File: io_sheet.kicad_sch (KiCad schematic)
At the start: 17 parts, among them J2 Conn_02x06_Top_Bottom, U1 PC817, U2 PC817, U3 PC817, U4 PC817, U5 PC817, U6 PC817, U7 PC817, U8 PC817

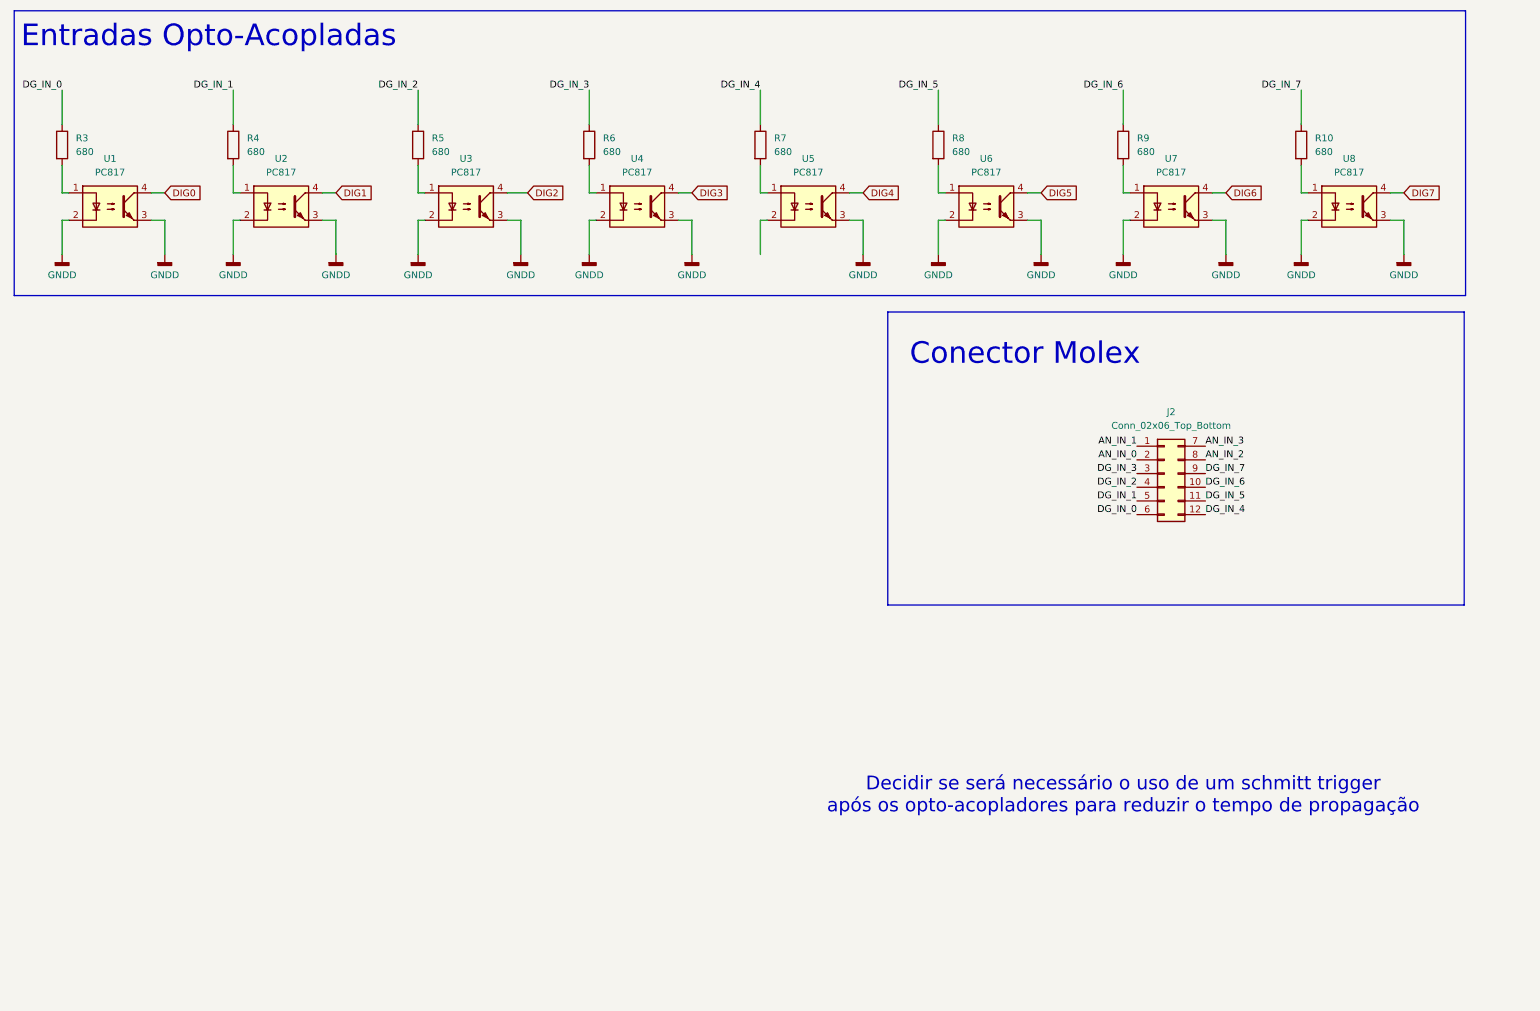
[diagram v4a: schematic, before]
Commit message: Alterei para ter 3 portas analogicas, adaptei o circuito do RPM para ter um jumper que permite usar como entrada digital
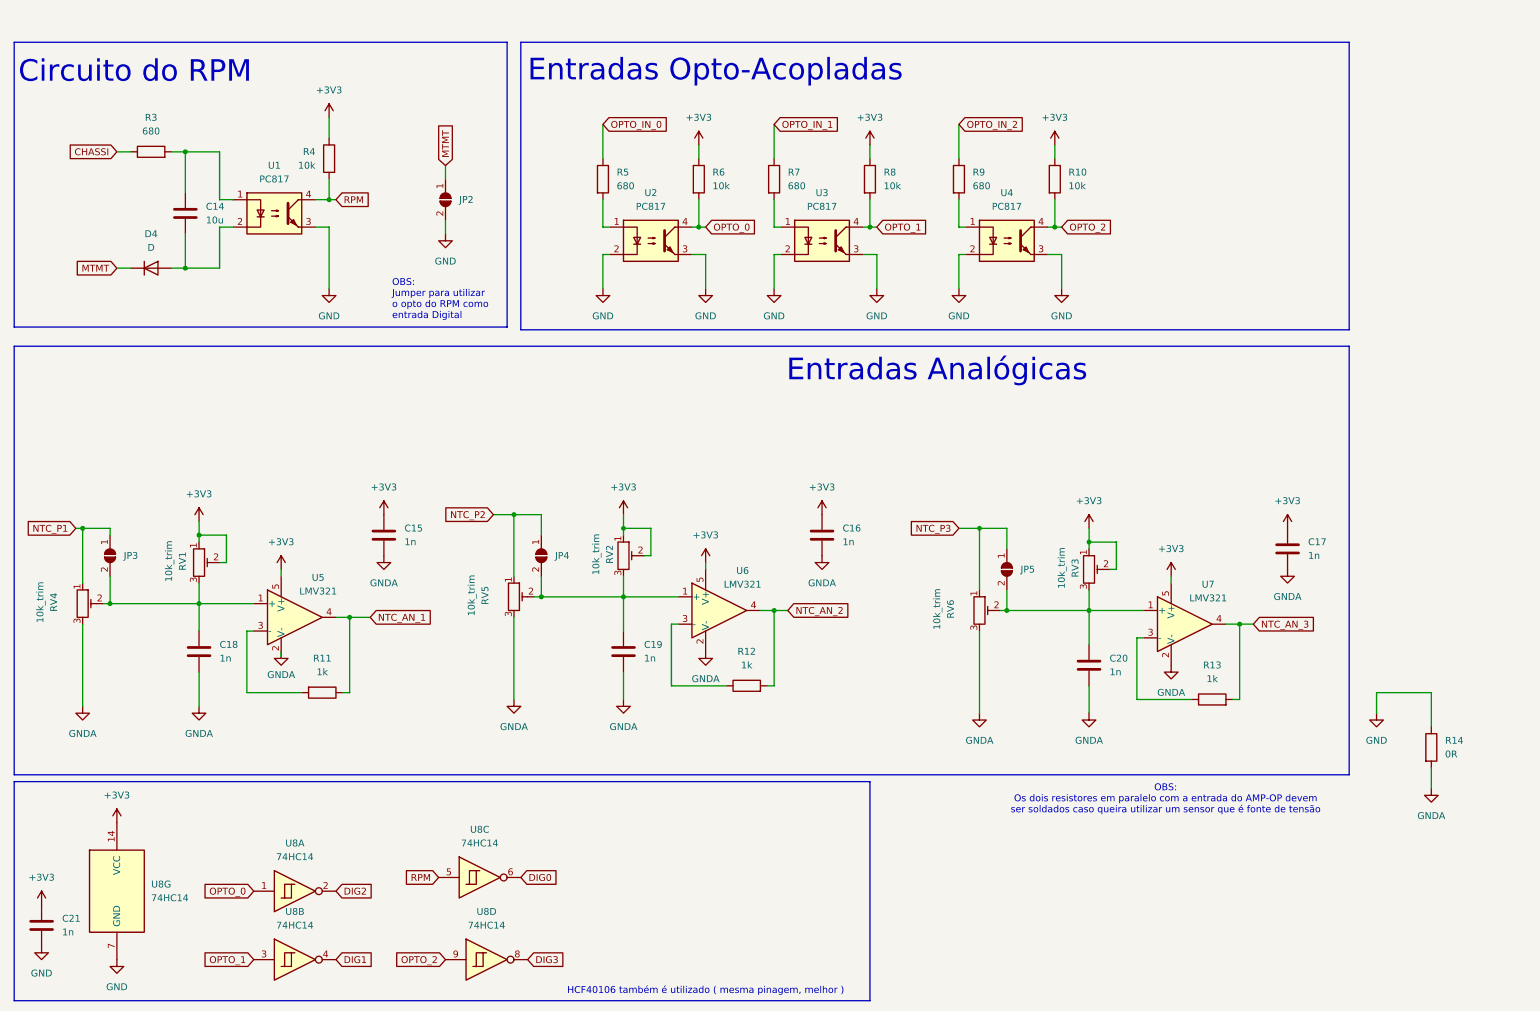
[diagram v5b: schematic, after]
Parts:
- removed J2: Conn_02x06_Top_Bottom, Baja_Library:MX120G, symbol Connector_Generic:Conn_02x06_Top_Bottom
- removed R5, R7: 680, Resistor_SMD:R_1206_3216Metric_Pad1.30x1.75mm_HandSolder, symbol Device:R
- removed U3, U5, U6, U7: PC817, Package_DIP:DIP-4_W7.62mm_SMDSocket_SmallPads, symbol Isolator:PC817
- removed U8: PC817, Baja_Library:SO-4_HandSoldering, symbol Isolator:PC817
- added C14: 10u, Capacitor_SMD:C_0603_1608Metric_Pad1.08x0.95mm_HandSolder, symbol Device:C
- added C15, C16, C17: 1n, symbol Device:C
- added C18, C19, C20, C21: 1n, Capacitor_SMD:C_0603_1608Metric_Pad1.08x0.95mm_HandSolder, symbol Device:C
- added D4: D, Diode_SMD:D_SMA_Handsoldering, symbol Device:D
- added JP2, JP3, JP4, JP5: SolderJumper_2_Open, Jumper:SolderJumper-2_P1.3mm_Open_RoundedPad1.0x1.5mm, symbol Jumper:SolderJumper_2_Open
- added R11, R12, R13: 1k, symbol Device:R
- added R14: 0R, Baja_Library:JumperPotencia, symbol Device:R
- added R3: 680, Resistor_SMD:R_1206_3216Metric_Pad1.30x1.75mm_HandSolder, symbol Device:R
- added R4: 10k, Resistor_SMD:R_1206_3216Metric_Pad1.30x1.75mm_HandSolder, symbol Device:R
- added RV1, RV2, RV3, RV4, RV5, RV6: 10k_trim, Potentiometer_THT:Potentiometer_Bourns_3296W_Vertical, symbol Device:R_Potentiometer_Trim
- added U1: PC817, Baja_Library:SO-4_HandSoldering, symbol Isolator:PC817
- added U5, U6, U7: LMV321, Package_TO_SOT_SMD:SOT-23-5_HandSoldering, symbol Amplifier_Operational:LMV321
- added U8: 74HC14, symbol 74xx:74HC14
- R10, R6, R8: value 680 -> 10k
- U2: renamed from U1; footprint Package_DIP:DIP-4_W7.62mm_SMDSocket_SmallPads -> Baja_Library:SO-4_HandSoldering
- U3: renamed from U2; footprint Package_DIP:DIP-4_W7.62mm_SMDSocket_SmallPads -> Baja_Library:SO-4_HandSoldering
- U4: footprint Package_DIP:DIP-4_W7.62mm_SMDSocket_SmallPads -> Baja_Library:SO-4_HandSoldering
- renumbered R3 to R5, R4 to R7
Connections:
- net DG_IN_5 is gone; now on net +3V3: R8.1
- net DG_IN_7 is gone; now on net +3V3: R10.1
- net DIG0: now also U8.6; no longer U2.4
- net DIG1: now also U8.4; no longer U3.4
- net DIG2: now also U8.2
- net DIG3: now also U8.8; no longer U4.4
- net OPTO_1: now reaches R8.2
- net OPTO_1: now also U3.4, U8.3
- net at R9.2: now also U4.1
- net OPTO_2: now reaches R10.2
- net OPTO_2: now also U4.4, U8.9
- net OPTO_0: now reaches R6.2
- net OPTO_0: now also U2.4, U8.1; no longer U4.1
- net DG_IN_0 renamed OPTO_IN_0
- net DG_IN_1 renamed OPTO_IN_1
- net DG_IN_3 renamed +3V3
- net +3V3: now also C15.1, C16.1, C17.1, C21.1, R4.1, RV1.1, RV1.2, RV2.1, RV2.2, RV3.1, RV3.2, U5.5 (V+), U6.5 (V+), U7.5 (V+), U8.14 (VCC)
- net DG_IN_6 renamed OPTO_IN_2
- net GNDD renamed GND
- net GND: now also C21.2, JP2.2 (B), R14.1, U1.3, U8.7 (GND)
- new net: C18.1, JP3.2 (B), RV1.3, RV4.2, U5.1 (+)
- new net: R11.2, U5.3 (-)
- new net: C20.1, JP5.2 (B), RV3.3, RV6.2, U7.1 (+)
- new net: C19.1, JP4.2 (B), RV2.3, RV5.2, U6.1 (+)
- new net: R12.1, U6.3 (-)
- new net: R13.1, U7.3 (-)
- new net: C14.2, D4.2 (A), U1.2
- new net: C14.1, R3.2, U1.1
- new net CHASSI: R3.1
- new net GNDA: C15.2, C16.2, C17.2, C18.2, C19.2, C20.2, R14.2, RV4.3, RV5.3, RV6.3, U5.2 (V-), U6.2 (V-), U7.2 (V-)
- new net MTMT: D4.1 (K), JP2.1 (A)
- new net NTC_AN_1: R11.1, U5.4
- new net NTC_AN_2: R12.2, U6.4
- new net NTC_AN_3: R13.2, U7.4
- new net NTC_P1: JP3.1 (A), RV4.1
- new net NTC_P2: JP4.1 (A), RV5.1
- new net NTC_P3: JP5.1 (A), RV6.1
- new net RPM: R4.2, U1.4, U8.5
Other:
- note added: "Circuito do RPM"
- note added: "Entradas Analógicas"
- note added: "HCF40106 também é utilizado ( mesma pinagem, melhor )"
- note added: "OBS: Jumper para utilizar o opto do RPM como entrada Digital"
- note added: "OBS: Os dois resistores em paralelo com a entrada do AMP-OP devem ser soldados caso queira utilizar um sensor que é fonte de tensão"
- note removed: "Conector Molex"
- note removed: "Decidir se será necessário o uso de um schmitt trigger após os opto-acopladores para reduzir o tempo de propagação"
- moved on the sheet: R5, R7, U2, U3

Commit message: Diminui o tamanho da placa
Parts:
- removed C15, C16, C17: 1n, symbol Device:C
- removed C19, C20: 1n, Capacitor_SMD:C_0603_1608Metric_Pad1.08x0.95mm_HandSolder, symbol Device:C
- removed JP3, JP4, JP5: SolderJumper_2_Open, Jumper:SolderJumper-2_P1.3mm_Open_RoundedPad1.0x1.5mm, symbol Jumper:SolderJumper_2_Open
- removed R14: 0R, Baja_Library:JumperPotencia, symbol Device:R
- removed RV4, RV5, RV6: 10k_trim, Potentiometer_THT:Potentiometer_Bourns_3296W_Vertical, symbol Device:R_Potentiometer_Trim
- removed U5, U6, U7: LMV321, Package_TO_SOT_SMD:SOT-23-5_HandSoldering, symbol Amplifier_Operational:LMV321
- added C13, C14: 1n, Capacitor_SMD:C_0603_1608Metric_Pad1.08x0.95mm_HandSolder, symbol Device:C
- added D4, D5, D6: D_Zener, Diode_SMD:D_SOD-123, symbol Device:D_Zener
- added JP6, JP7, JP8: SolderJumper_2_Open, Jumper:SolderJumper-2_P1.3mm_Open_RoundedPad1.0x1.5mm, symbol Jumper:SolderJumper_2_Open
- C11: renamed from C14; footprint Capacitor_SMD:C_0603_1608Metric_Pad1.08x0.95mm_HandSolder -> Capacitor_SMD:C_0805_2012Metric_Pad1.18x1.45mm_HandSolder
- R11, R12, R13: value 1k -> 27k; footprint (none) -> Resistor_SMD:R_1206_3216Metric_Pad1.30x1.75mm_HandSolder
- renumbered C18 to C12, C21 to C15, D4 to D3, U8 to U5
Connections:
- net GNDA is gone; now on net GND: C12.2
- net +3V3: now also R11.1, R12.1, R13.1; no longer RV1.1, RV1.2, RV2.1, RV2.2, RV3.1, RV3.2
- net DIG0: now also U5.8; no longer U5.6
- net DIG1: now also U5.6; no longer U5.4
- net DIG2: now also U5.4; no longer U5.2
- net DIG3: now also U5.2; no longer U5.8
- net GND: now also RV1.3, RV2.3, RV3.3, C13.2, C14.2, D4.2 (A), D5.2 (A), D6.2 (A)
- net NTC_AN_1: now also C12.1, R11.2, RV2.2, D4.1 (K), JP6.2 (B); no longer R11.1
- net NTC_AN_2: now also RV3.2, C13.1, D5.1 (K), JP7.2 (B)
- net NTC_AN_3: now also RV1.2, C14.1, D6.1 (K), JP8.2 (B)
- net NTC_P1: now also RV2.1, JP6.1 (A)
- net NTC_P2: now also RV3.1, JP7.1 (A)
- net NTC_P3: now also RV1.1, JP8.1 (A)
- net OPTO_2: now also U5.5; no longer U5.9
- net RPM: now also U5.9; no longer U5.5
- net JMP_RPM: now reaches C11.2, D3.2 (A), U1.2
- net JMP_RPM: now also JP2.1 (A)
- net CHASSI renamed MT-
- net MTMT renamed MT+
- net MT+: no longer JP2.1 (A)
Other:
- note added: "R11,R12 e R13 são para leitura de NTC/PTC ou qualquer outro sensor resistivo"
- note removed: "OBS: Os dois resistores em paralelo com a entrada do AMP-OP devem ser soldados caso queira utilizar um sensor que é fonte de tensão"
- moved on the sheet: C12
